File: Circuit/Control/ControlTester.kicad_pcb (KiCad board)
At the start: 2 copper layers, 17.8 x 43.2 mm, 13 parts, among them J1 Power, J2 Signal, J3 12V NO G

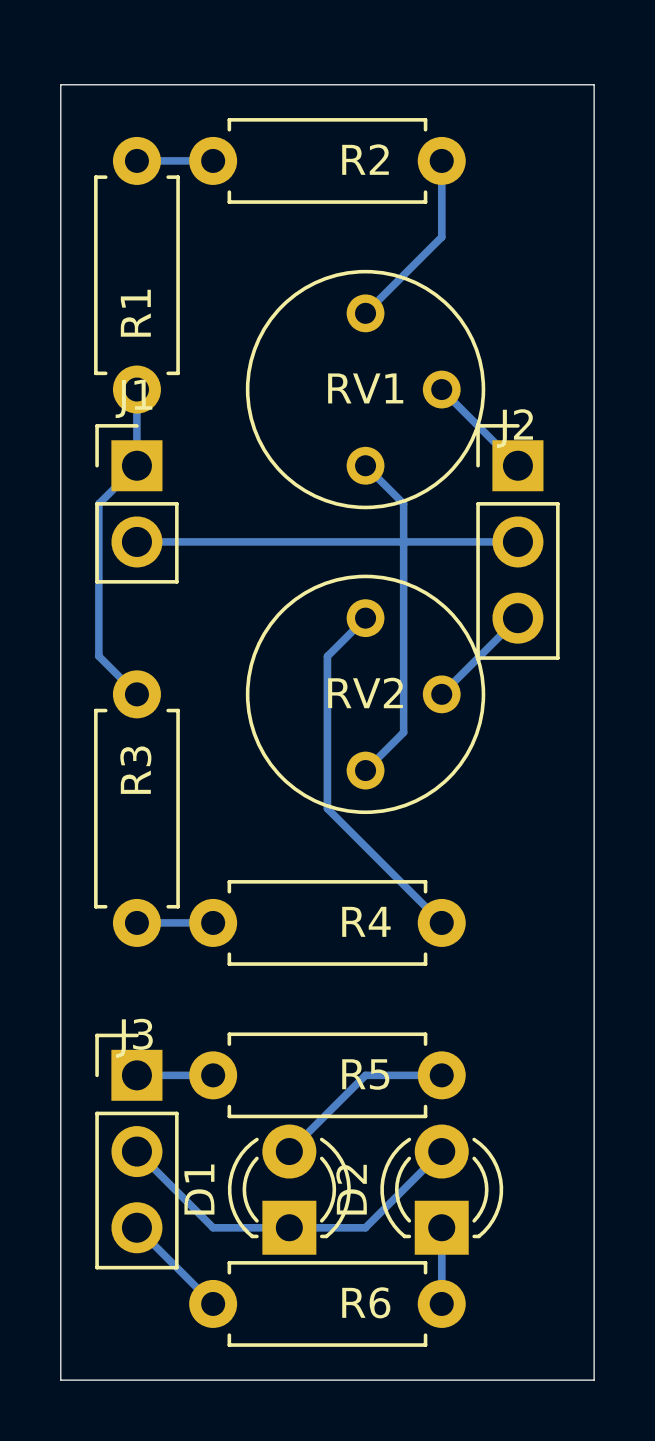
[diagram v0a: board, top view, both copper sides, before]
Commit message: [Circuit] Update the control test module to use on the new control module
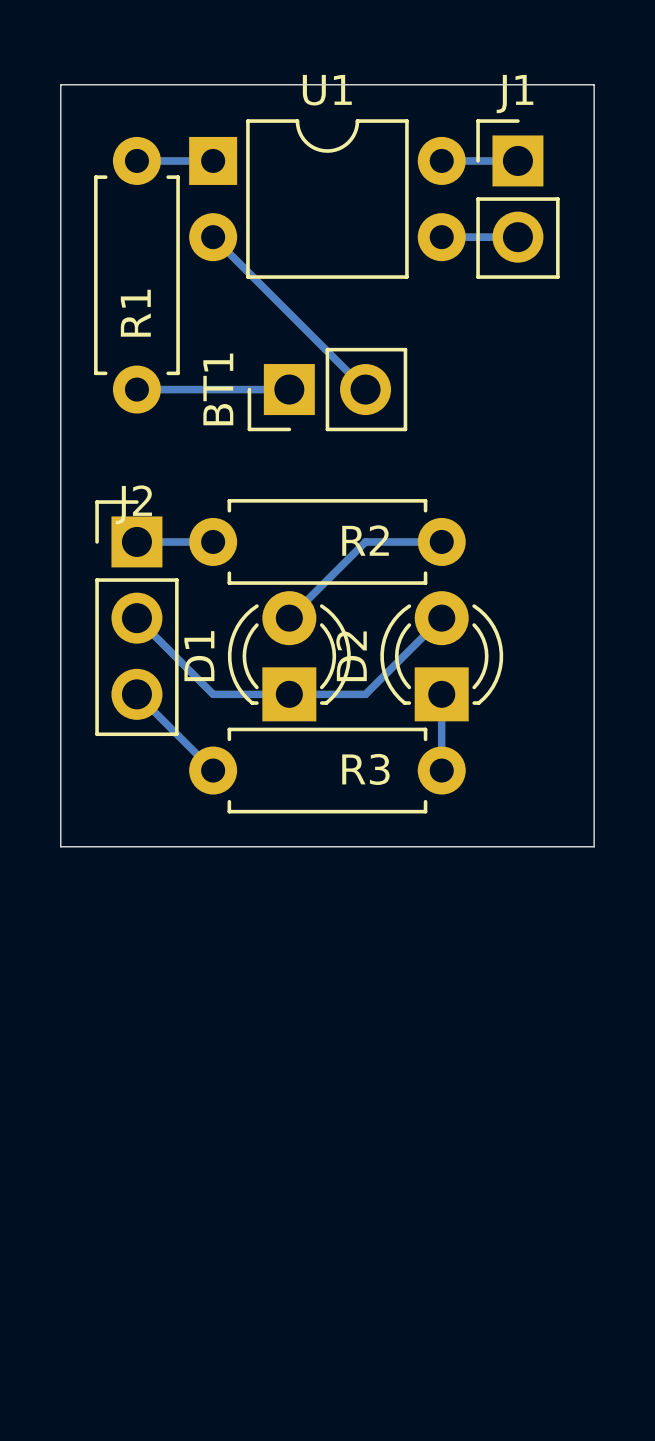
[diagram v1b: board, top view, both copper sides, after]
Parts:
- removed the J1 at (81.3, 66.0)
- removed the R2 at (83.8, 55.9)
- removed the R3 at (81.3, 73.7)
- removed R4: 20K, Resistor_THT:R_Axial_DIN0207_L6.3mm_D2.5mm_P7.62mm_Horizontal
- removed RV1, RV2: 50K, Potentiometer_THT:Potentiometer_Bourns_3339P_Vertical
- added BT1: 12V Battery, Connector_PinHeader_2.54mm:PinHeader_1x02_P2.54mm_Vertical, F.Cu at (86.4, 63.5)
- added U1: PC817, Package_DIP:DIP-4_W7.62mm, F.Cu at (83.8, 55.9)
- J1: renamed from J2; footprint Connector_PinHeader_2.54mm:PinHeader_1x03_P2.54mm_Vertical -> Connector_PinHeader_2.54mm:PinHeader_1x02_P2.54mm_Vertical
- R1: value 20K -> 1K
- moved D1 17.8 mm to (86.4, 73.7)
- moved D2 17.8 mm to (91.4, 73.7)
- moved J2 17.8 mm to (81.3, 68.6)
- moved R2 17.8 mm to (83.8, 68.6)
- moved R3 17.8 mm to (83.8, 76.2)
- moved J1 10.2 mm to (94.0, 55.9)
- renumbered J3 to J2, R5 to R2, R6 to R3
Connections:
- J1 pad 2: GND -> Net-(J1-Pad2)
- R1 pad 1: +12V -> Net-(BT1-Pad1)
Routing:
- net GND: track 23.9 -> 0.00 mm
- net Net-(R4-Pad2): track 12.3 -> 0.00 mm
- net +12V: track 11.2 -> 0.00 mm
- net Net-(BT1-Pad2): track 0.00 -> 7.18 mm
- net Net-(R2-Pad2): track 6.13 -> 0.00 mm
- net Net-(BT1-Pad1): track 0.00 -> 5.08 mm
- net Net-(J2-Pad3) (its old number): track 3.59 -> 0.00 mm
- net Net-(J1-Pad2): track 0.00 -> 2.54 mm
- net Net-(R3-Pad2): track 2.54 -> 0.00 mm
- net Net-(J1-Pad1): track 3.59 -> 2.54 mm
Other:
- board size 17.8 x 43.2 mm -> 17.8 x 25.4 mm

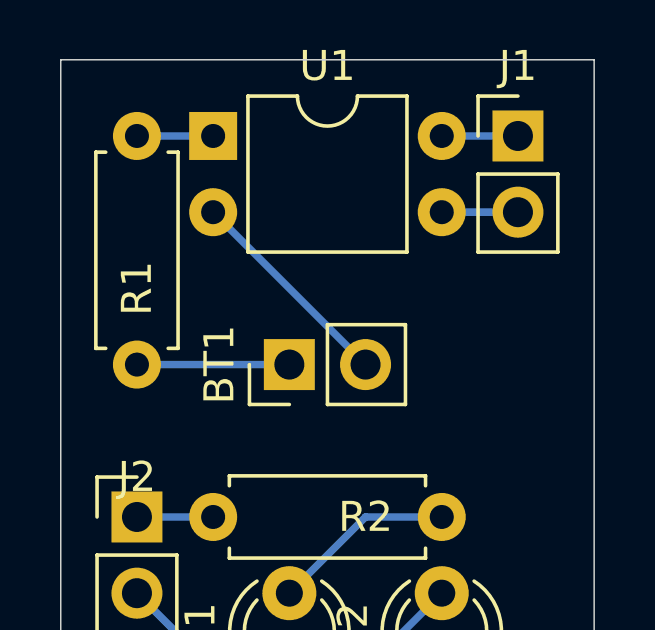
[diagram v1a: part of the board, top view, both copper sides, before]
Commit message: [Circuit] Optimize the interface between capacitor bank modules and voltage sensing module
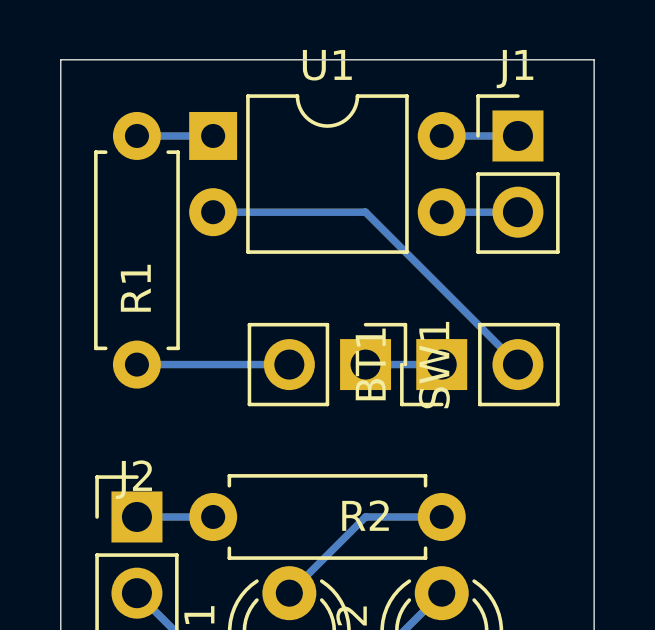
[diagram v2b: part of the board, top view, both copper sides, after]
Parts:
- added SW1: SW_Push, Connector_PinHeader_2.54mm:PinHeader_1x02_P2.54mm_Vertical, F.Cu at (88.9, 63.5)
- moved BT1 5.08 mm to (91.4, 63.5)
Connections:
- R1 pad 1: Net-(BT1-Pad1) -> Net-(R1-Pad1)
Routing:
- net Net-(BT1-Pad2): track 7.18 -> 12.3 mm
- net Net-(R1-Pad1): track 0.00 -> 5.08 mm
- net Net-(BT1-Pad1): track 5.08 -> 2.54 mm
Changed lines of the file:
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@@
     (thickness 1.6)
     (drawings 4)
-    (tracks 14)
+    (tracks 16)
     (zones 0)
-    (modules 9)
-    (nets 11)
+    (modules 10)
+    (nets 12)
   )
   (page A4)
@@
   (net 9 "Net-(J1-Pad2)")
   (net 10 "Net-(J1-Pad1)")
+  (net 11 "Net-(R1-Pad1)")
   (net_class Default "This is the default net class."
     (clearance 0.2)
@@
     (add_net "Net-(J2-Pad1)")
     (add_net "Net-(J2-Pad3)")
+    (add_net "Net-(R1-Pad1)")
     (add_net "Net-(R1-Pad2)")
+  )
+  (module Connector_PinHeader_2.54mm:PinHeader_1x02_P2.54mm_Vertical (layer F.Cu)
+    (at 88.9 63.5 270)
+    (descr "Through hole straight pin header, 1x02, 2.54mm pitch, single row")
+    (tags "Through hole pin header THT 1x02 2.54mm single row")
+    (fp_text reference SW1 (at 0 -2.33 90) (layer F.SilkS)
+      (effects (font (size 1 1) (thickness 0.15)))
+    )
+    (fp_text value SW_Push (at 0 4.87 90) (layer F.Fab)
+      (effects (font (size 1 1) (thickness 0.15)))
+    )
+    (fp_text user %R (at 0 1.27) (layer F.Fab)
+      (effects (font (size 1 1) (thickness 0.15)))
+    )
+    (fp_line (start 1.8 -1.8) (end -1.8 -1.8) (layer F.CrtYd) (width 0.05))
+    (fp_line (start 1.8 4.35) (end 1.8 -1.8) (layer F.CrtYd) (width 0.05))
+    (fp_line (start -1.8 4.35) (end 1.8 4.35) (layer F.CrtYd) (width 0.05))
+    (fp_line (start -1.8 -1.8) (end -1.8 4.35) (layer F.CrtYd) (width 0.05))
+    (fp_line (start -1.33 -1.33) (end 0 -1.33) (layer F.SilkS) (width 0.12))
+    (fp_line (start -1.33 0) (end -1.33 -1.33) (layer F.SilkS) (width 0.12))
+    (fp_line (start -1.33 1.27) (end 1.33 1.27) (layer F.SilkS) (width 0.12))
+    (fp_line (start 1.33 1.27) (end 1.33 3.87) (layer F.SilkS) (width 0.12))
+    (fp_line (start -1.33 1.27) (end -1.33 3.87) (layer F.SilkS) (width 0.12))
+    (fp_line (start -1.33 3.87) (end 1.33 3.87) (layer F.SilkS) (width 0.12))
+    (fp_line (start -1.27 -0.635) (end -0.635 -1.27) (layer F.Fab) (width 0.1))
+    (fp_line (start -1.27 3.81) (end -1.27 -0.635) (layer F.Fab) (width 0.1))
+    (fp_line (start 1.27 3.81) (end -1.27 3.81) (layer F.Fab) (width 0.1))
+    (fp_line (start 1.27 -1.27) (end 1.27 3.81) (layer F.Fab) (width 0.1))
+    (fp_line (start -0.635 -1.27) (end 1.27 -1.27) (layer F.Fab) (width 0.1))
+    (pad 2 thru_hole oval (at 0 2.54 270) (size 1.7 1.7) (drill 1) (layers *.Cu *.Mask)
+      (net 11 "Net-(R1-Pad1)"))
+    (pad 1 thru_hole rect (at 0 0 270) (size 1.7 1.7) (drill 1) (layers *.Cu *.Mask)
+      (net 8 "Net-(BT1-Pad1)"))
+    (model ${KISYS3DMOD}/Connector_PinHeader_2.54mm.3dshapes/PinHeader_1x02_P2.54mm_Vertical.wrl
+      (at (xyz 0 0 0))
+      (scale (xyz 1 1 1))
+      (rotate (xyz 0 0 0))
+    )
   )
   (module Package_DIP:DIP-4_W7.62mm (layer F.Cu)
@@
   )
   (module Connector_PinHeader_2.54mm:PinHeader_1x02_P2.54mm_Vertical (layer F.Cu)
-    (at 86.36 63.5 90)
+    (at 91.44 63.5 90)
     (descr "Through hole straight pin header, 1x02, 2.54mm pitch, single row")
     (tags "Through hole pin header THT 1x02 2.54mm single row")
@@
       (net 4 "Net-(R1-Pad2)"))
     (pad 1 thru_hole circle (at 0 0 90) (size 1.6 1.6) (drill 0.8) (layers *.Cu *.Mask)
-      (net 8 "Net-(BT1-Pad1)"))
+      (net 11 "Net-(R1-Pad1)"))
     (model ${KISYS3DMOD}/Resistor_THT.3dshapes/R_Axial_DIN0207_L6.3mm_D2.5mm_P7.62mm_Horizontal.wrl
       (at (xyz 0 0 0))
@@
   (segment (start 88.9 73.66) (end 91.44 71.12) (width 0.25) (layer B.Cu) (net 5) (status 20))
   (segment (start 91.44 73.66) (end 91.44 76.2) (width 0.25) (layer B.Cu) (net 6) (status 30))
-  (segment (start 83.82 58.42) (end 88.9 63.5) (width 0.25) (layer B.Cu) (net 7))
-  (segment (start 86.36 63.5) (end 81.28 63.5) (width 0.25) (layer B.Cu) (net 8))
+  (segment (start 93.98 63.5) (end 88.9 58.42) (width 0.25) (layer B.Cu) (net 7))
+  (segment (start 88.9 58.42) (end 83.82 58.42) (width 0.25) (layer B.Cu) (net 7))
+  (segment (start 88.9 63.5) (end 91.44 63.5) (width 0.25) (layer B.Cu) (net 8))
   (segment (start 91.44 58.42) (end 93.98 58.42) (width 0.25) (layer B.Cu) (net 9))
   (segment (start 91.44 55.88) (end 93.98 55.88) (width 0.25) (layer B.Cu) (net 10))
+  (segment (start 81.28 63.5) (end 86.36 63.5) (width 0.25) (layer B.Cu) (net 11))
 )
